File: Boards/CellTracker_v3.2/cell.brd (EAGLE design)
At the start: 41.9 x 41.9 mm, 24 parts, among them U2 LMR16020

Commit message: Changing antenna conf
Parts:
- moved U$8 2.17 mm to (40.3, 25.2), turned to 0 degrees
- moved U$7 1.80 mm to (28.7, 28.5)
- moved R2 0.57 mm to (20.7, 31.8)
- moved R6 0.57 mm to (20.7, 29.8)
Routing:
- net +3V3: track 61.2 -> 63.6 mm
- net N$1: track 5.25 -> 3.63 mm
- net N$4: track 3.62 -> 2.26 mm
- net N$3: track 3.29 -> 2.71 mm
- net RX3: track 13.5 -> 14.1 mm
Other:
- board size 41.9 x 41.9 mm -> 44.7 x 41.9 mm

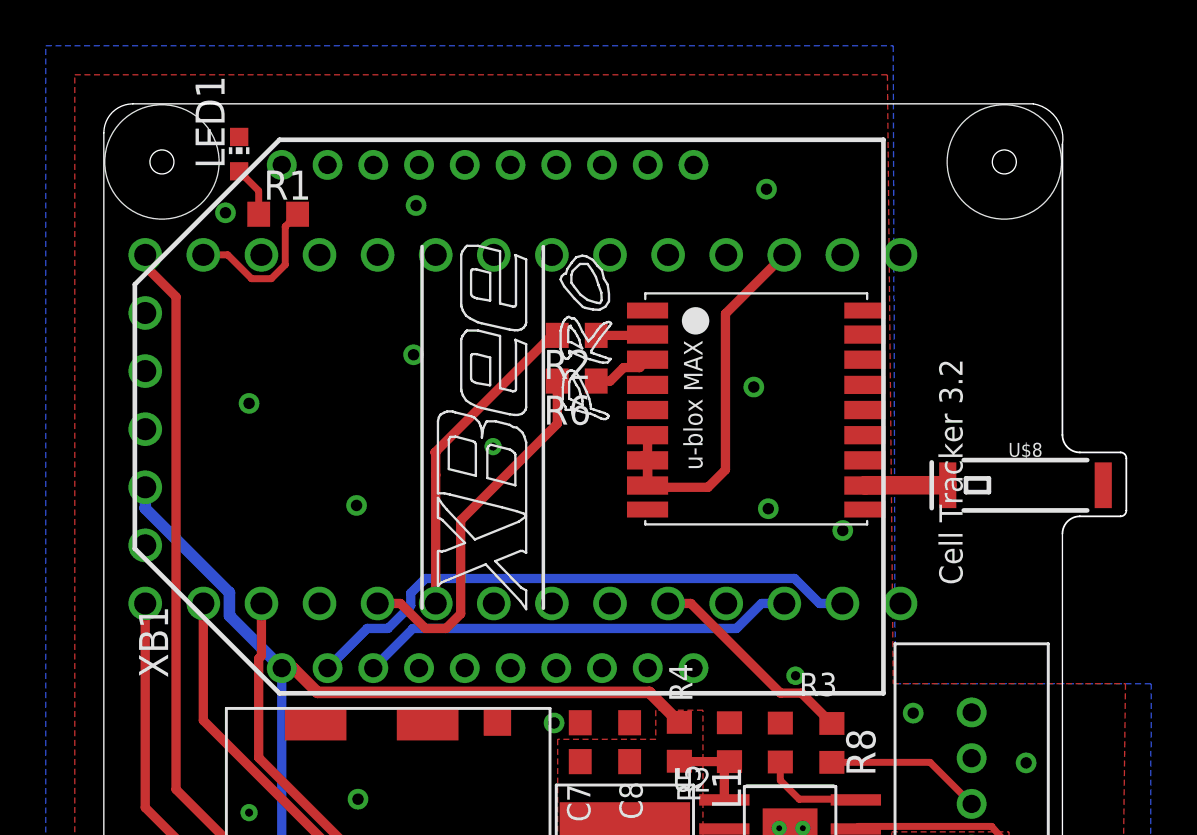
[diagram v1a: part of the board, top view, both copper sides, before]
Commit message: updating resistors for correct cutoff
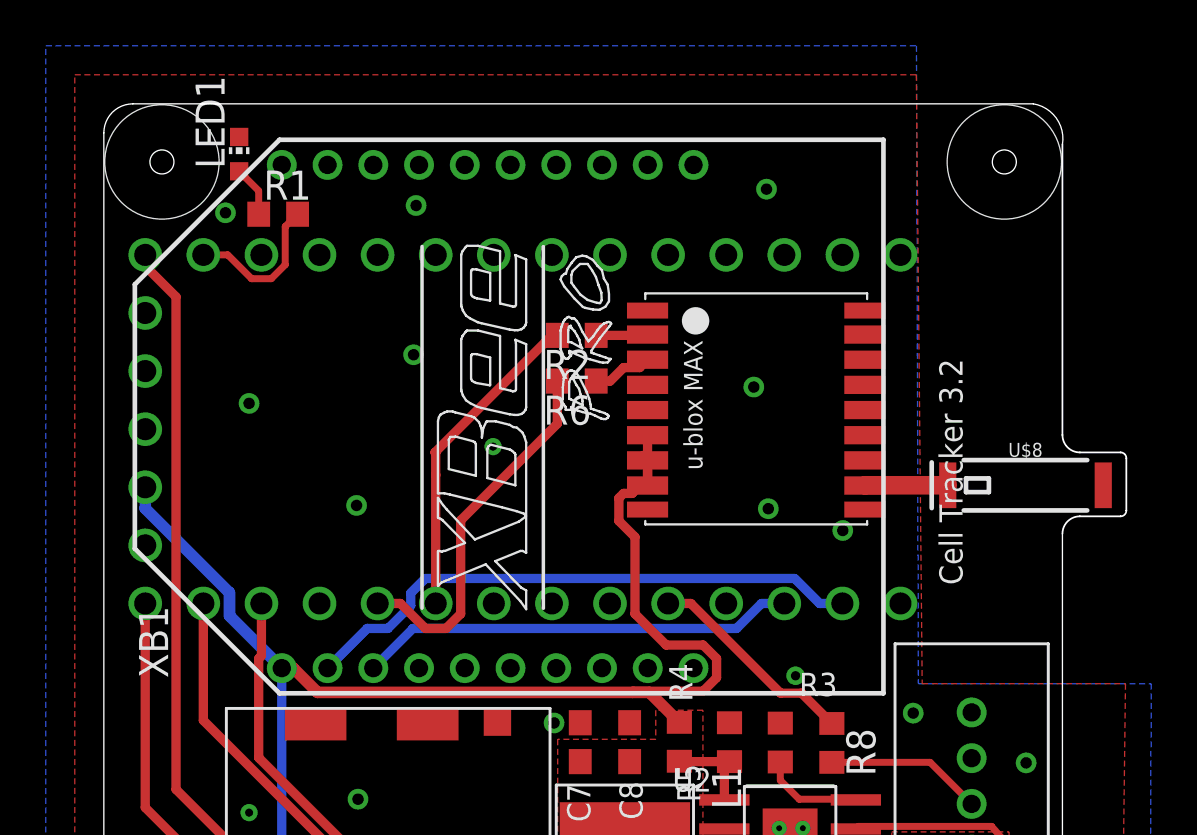
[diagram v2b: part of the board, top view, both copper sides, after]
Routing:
- net +3V3: track 63.6 -> 65.0 mm
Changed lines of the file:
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@@
 <polygon width="0.4064" layer="16" rank="6">
 <vertex x="-2.54" y="44.45"/>
-<vertex x="34.51225" y="44.45"/>
-<vertex x="34.597028125" y="16.557625"/>
+<vertex x="35.527478125" y="44.45"/>
+<vertex x="35.61225625" y="16.557625"/>
 <vertex x="45.792615625" y="16.557625"/>
 <vertex x="45.72" y="-2.54"/>
@@
 <polygon width="0.4064" layer="1" rank="6">
 <vertex x="-1.27" y="43.18"/>
-<vertex x="34.25825" y="43.18"/>
-<vertex x="34.513415625" y="16.557625"/>
+<vertex x="35.52338125" y="43.18"/>
+<vertex x="35.778546875" y="16.557625"/>
 <vertex x="44.66653125" y="16.557625"/>
 <vertex x="44.45" y="-1.27"/>
@@
 <contactref element="C7" pad="1"/>
 <contactref element="U$3" pad="VDD"/>
-<wire x1="23.77175" y1="26.32275" x2="23.77175" y2="25.146" width="0.4064" layer="1"/>
+<wire x1="23.77175" y1="25.146" x2="23.77175" y2="26.32275" width="0.4064" layer="1"/>
 <wire x1="23.77175" y1="26.32275" x2="23.77175" y2="27.42275" width="0.4064" layer="1"/>
 <wire x1="25.161875" y1="14.867625" x2="23.85065" y2="16.17885" width="0.508" layer="1"/>
 <wire x1="8.2803625" y1="17.23925" x2="7.78" y2="17.23925" width="0.508" layer="1"/>
-<wire x1="23.85065" y1="16.17885" x2="9.3407625" y2="16.17885" width="0.508" layer="1"/>
+<wire x1="23.85065" y1="16.17885" x2="23.114" y2="16.17885" width="0.508" layer="1"/>
+<wire x1="23.114" y1="16.17885" x2="9.3407625" y2="16.17885" width="0.508" layer="1"/>
 <wire x1="9.3407625" y1="16.17885" x2="8.2803625" y2="17.23925" width="0.508" layer="1"/>
 <wire x1="7.78" y1="17.23925" x2="7.78" y2="8.73" width="0.4064" layer="16"/>
@@
 <wire x1="5.492625" y1="19.526625" x2="5.492625" y2="20.5397" width="0.508" layer="16"/>
 <wire x1="5.492625" y1="20.5397" x2="1.809625" y2="24.2227" width="0.508" layer="16"/>
-<wire x1="29.749625" y1="35.30625" x2="27.178" y2="32.734625" width="0.4064" layer="1"/>
-<wire x1="27.178" y1="32.734625" x2="27.178" y2="25.908" width="0.4064" layer="1"/>
-<wire x1="27.178" y1="25.908" x2="26.416" y2="25.146" width="0.4064" layer="1"/>
-<wire x1="26.416" y1="25.146" x2="23.77175" y2="25.146" width="0.4064" layer="1"/>
-<wire x1="23.85065" y1="16.17885" x2="23.77175" y2="25.22275" width="0" layer="19" extent="1-1"/>
+<wire x1="26.19819375" y1="16.22965" x2="26.7896" y2="16.82105625" width="0.4064" layer="1"/>
+<wire x1="26.7896" y1="16.82105625" x2="26.7896" y2="17.65744375" width="0.4064" layer="1"/>
+<wire x1="26.7896" y1="17.65744375" x2="26.19819375" y2="18.24885" width="0.4064" layer="1"/>
+<wire x1="22.51615" y1="23.67545625" x2="22.51615" y2="24.67004375" width="0.4064" layer="1"/>
+<wire x1="22.51615" y1="24.67004375" x2="22.72445625" y2="24.87835" width="0.4064" layer="1"/>
+<wire x1="23.114" y1="16.17885" x2="23.1648" y2="16.22965" width="0.4064" layer="1"/>
+<wire x1="22.72445625" y1="24.87835" x2="23.10035" y2="24.87835" width="0.4064" layer="1"/>
+<wire x1="23.1648" y1="16.22965" x2="26.19819375" y2="16.22965" width="0.4064" layer="1"/>
+<wire x1="26.19819375" y1="18.24885" x2="24.58681875" y2="18.24885" width="0.4064" layer="1"/>
+<wire x1="24.58681875" y1="18.24885" x2="23.221825" y2="19.61384375" width="0.4064" layer="1"/>
+<wire x1="23.221825" y1="19.61384375" x2="23.221825" y2="22.96978125" width="0.4064" layer="1"/>
+<wire x1="23.221825" y1="22.96978125" x2="22.51615" y2="23.67545625" width="0.4064" layer="1"/>
+<wire x1="23.10035" y1="24.87835" x2="23.368" y2="25.146" width="0.4064" layer="1"/>
+<wire x1="23.77175" y1="27.42275" x2="29.749625" y2="35.30625" width="0" layer="19" extent="1-1"/>
+<wire x1="23.368" y1="25.146" x2="23.77175" y2="25.146" width="0" layer="19" extent="1-1"/>
+<wire x1="22.987" y1="13.15175" x2="25.161875" y2="14.867625" width="0" layer="19" extent="1-1"/>
+<wire x1="20.828" y1="13.15175" x2="22.987" y2="13.15175" width="0" layer="19" extent="1-1"/>
+<wire x1="22.780625" y1="10.528125" x2="22.987" y2="13.15175" width="0" layer="19" extent="1-1"/>
 </signal>
 <signal name="RX3">

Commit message: Code+nearly completed boards
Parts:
- added C1: (no value), jmolterLib:ELNASUPERCAP
- added D1: RB520S30T1G, diode:SOD523
- added R7: 22, resistor:R0603
- C6: value 47 uF -> 0.1 uF
- R10: value 195k -> 140k
- R4: value 45k -> 340k
- R5: value 13.3k -> 100k
- R9: value 45k -> 30.1k
- moved R6 0.08 mm to (20.7, 29.7)
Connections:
- new net N$11: D1.C, R7.2
- new net N$5: C1.3V3, R7.1, U$7.6_V_BCKP
- net +3V3: now also D1.A; no longer U$7.6_V_BCKP
- net GND: now also C1.GND
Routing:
- net +3V3: track 65.0 -> 79.8 mm
- net N$5: track 0.00 -> 14.4 mm, vias 0 -> 2
- net N$11: track 0.00 -> 1.98 mm
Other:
- outline, holes or cut-outs redrawn

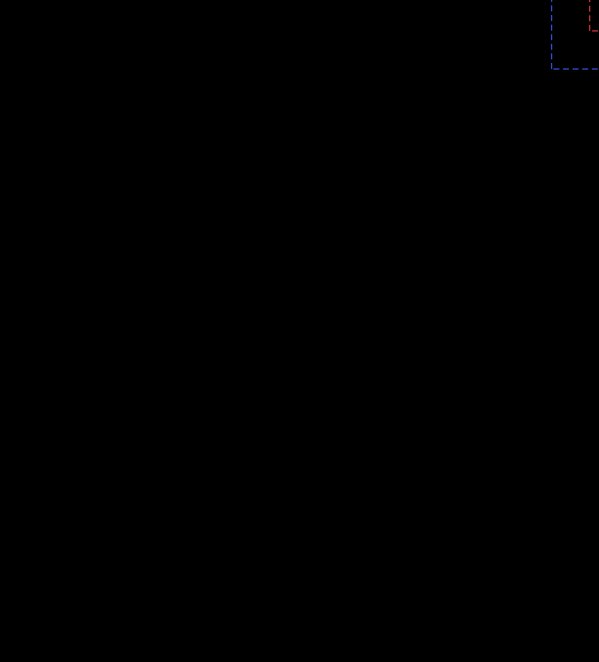
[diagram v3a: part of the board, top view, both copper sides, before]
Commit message: Moved libs, adding isolator
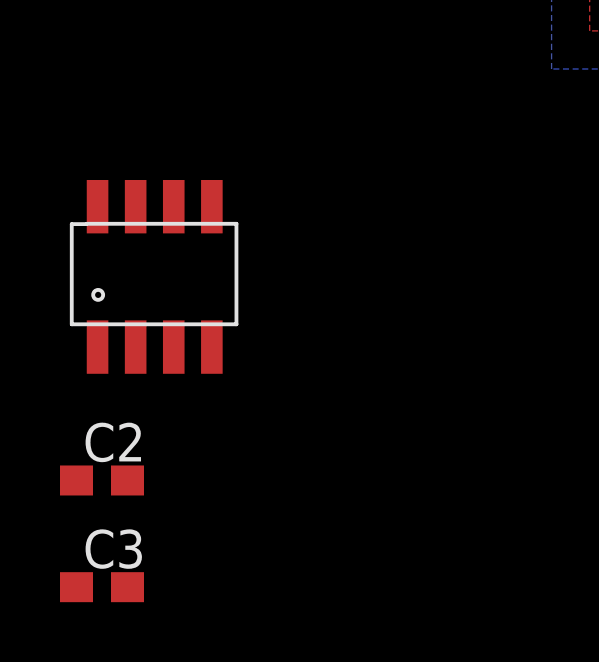
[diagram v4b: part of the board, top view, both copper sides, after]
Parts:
- added C2, C3: 0.1uF, rcl:C0603
- added ISO7021: ISO7021, jmolterLib:8-SOIC
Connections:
- removed net N$6: U$1.VIN
- new net GND_EX: C3.2, ISO7021.P$5
- new net IN_A: ISO7021.P$7
- new net IS_RX: ISO7021.P$2
- new net IS_TX: ISO7021.P$3
- new net OUT_B: ISO7021.P$6
- new net VCC_EX: C3.1, ISO7021.P$8
- net +3V3: now also C2.1, ISO7021.P$1
- net GND: now also C2.2, ISO7021.P$4
- net VIN: now also U$1.VIN
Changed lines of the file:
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@@
 <attribute name="VALUE" x="13.843" y="30.607" size="1.27" layer="27"/>
+</element>
+<element name="ISO7021" library="jmolterLib" package="8-SOIC" value="ISO7021" x="-18.034" y="-12.7" smashed="yes"/>
+<element name="C2" library="rcl" library_urn="urn:adsk.eagle:library:334" package="C0603" package3d_urn="urn:adsk.eagle:package:23616/2" value="0.1uF" x="-17.526" y="-16.256" smashed="yes">
+<attribute name="NAME" x="-18.161" y="-15.621" size="1.27" layer="25"/>
+<attribute name="SPICEPREFIX" value="C" x="-17.526" y="-16.256" size="1.778" layer="27" display="off"/>
+<attribute name="VALUE" x="-18.161" y="-18.161" size="1.27" layer="27"/>
+</element>
+<element name="C3" library="rcl" library_urn="urn:adsk.eagle:library:334" package="C0603" package3d_urn="urn:adsk.eagle:package:23616/2" value="0.1uF" x="-17.526" y="-19.812" smashed="yes">
+<attribute name="NAME" x="-18.161" y="-19.177" size="1.27" layer="25"/>
+<attribute name="SPICEPREFIX" value="C" x="-17.526" y="-19.812" size="1.778" layer="27" display="off"/>
+<attribute name="VALUE" x="-18.161" y="-21.717" size="1.27" layer="27"/>
 </element>
 </elements>
@@
 <via x="17.018" y="26.924" extent="1-16" drill="0.35"/>
 <contactref element="C1" pad="GND"/>
+<contactref element="ISO7021" pad="P$4"/>
+<contactref element="C2" pad="2"/>
+<wire x1="23.77175" y1="32.87275" x2="28.971875" y2="38.179375" width="0" layer="19" extent="1-1"/>
+<wire x1="28.41625" y1="29.5275" x2="23.77175" y2="32.87275" width="0" layer="19" extent="1-1"/>
+<wire x1="29.05125" y1="24.209375" x2="28.41625" y2="29.5275" width="0" layer="19" extent="1-1"/>
+<wire x1="32.305625" y1="23.256875" x2="29.05125" y2="24.209375" width="0" layer="19" extent="1-1"/>
+<wire x1="33.27175" y1="24.17275" x2="32.305625" y2="23.256875" width="0" layer="19" extent="1-1"/>
+<wire x1="33.27175" y1="26.32275" x2="33.27175" y2="24.17275" width="0" layer="19" extent="1-1"/>
+<wire x1="34.829625" y1="20.06625" x2="32.305625" y2="23.256875" width="0" layer="19" extent="1-1"/>
+<wire x1="35.385375" y1="15.27175" x2="34.829625" y2="20.06625" width="0" layer="19" extent="1-1"/>
+<wire x1="37.94125" y1="15.303125" x2="35.385375" y2="15.27175" width="0" layer="19" extent="1-1"/>
+<wire x1="37.94125" y1="13.303125" x2="37.94125" y2="15.303125" width="0" layer="19" extent="1-1"/>
+<wire x1="40.3225" y1="13.096875" x2="37.94125" y2="13.303125" width="0" layer="19" extent="1-1"/>
+<wire x1="29.575125" y1="14.835875" x2="35.385375" y2="15.27175" width="0" layer="19" extent="1-1"/>
+<wire x1="28.717875" y1="16.652875" x2="29.575125" y2="14.835875" width="0" layer="19" extent="1-1"/>
+<wire x1="27.352625" y1="14.85175" x2="29.575125" y2="14.835875" width="0" layer="19" extent="1-1"/>
+<wire x1="25.78" y1="17.23925" x2="27.352625" y2="14.85175" width="0" layer="19" extent="1-1"/>
+<wire x1="22.987" y1="14.85175" x2="25.78" y2="17.23925" width="0" layer="19" extent="1-1"/>
+<wire x1="20.828" y1="14.85175" x2="22.987" y2="14.85175" width="0" layer="19" extent="1-1"/>
+<wire x1="19.685" y1="14.843125" x2="20.828" y2="14.85175" width="0" layer="19" extent="1-1"/>
+<wire x1="17.2075" y1="14.878125" x2="19.685" y2="14.843125" width="0" layer="19" extent="1-1"/>
+<wire x1="14.1575" y1="14.778125" x2="17.2075" y2="14.878125" width="0" layer="19" extent="1-1"/>
+<wire x1="11.1125" y1="11.509375" x2="14.1575" y2="14.778125" width="0" layer="19" extent="1-1"/>
+<wire x1="9.2575" y1="14.778125" x2="11.1125" y2="11.509375" width="0" layer="19" extent="1-1"/>
+<wire x1="29.5275" y1="10.239375" x2="29.575125" y2="14.835875" width="0" layer="19" extent="1-1"/>
+<wire x1="29.5275" y1="9.445625" x2="29.5275" y2="10.239375" width="0" layer="19" extent="1-1"/>
+<wire x1="30.00375" y1="9.55675" x2="29.5275" y2="9.445625" width="0" layer="19" extent="1-1"/>
+<wire x1="30.559375" y1="9.445625" x2="30.00375" y2="9.55675" width="0" layer="19" extent="1-1"/>
+<wire x1="29.272625" y1="8.90675" x2="29.5275" y2="9.445625" width="0" layer="19" extent="1-1"/>
+<wire x1="30.559375" y1="10.239375" x2="30.559375" y2="9.445625" width="0" layer="19" extent="1-1"/>
+<wire x1="30.559375" y1="8.651875" x2="30.559375" y2="9.445625" width="0" layer="19" extent="1-1"/>
+<wire x1="6.35" y1="10.922" x2="11.1125" y2="11.509375" width="0" layer="19" extent="1-1"/>
+<wire x1="28.971875" y1="2.75925" x2="29.5275" y2="8.651875" width="0" layer="19" extent="1-1"/>
+<wire x1="32.131" y1="2.75925" x2="28.971875" y2="2.75925" width="0" layer="19" extent="1-1"/>
+<wire x1="34.471875" y1="2.778125" x2="32.131" y2="2.75925" width="0" layer="19" extent="1-1"/>
+<wire x1="6.111875" y1="4.7625" x2="6.35" y2="10.922" width="0" layer="19" extent="1-1"/>
+<wire x1="5.7575" y1="2.578125" x2="6.111875" y2="4.7625" width="0" layer="19" extent="1-1"/>
+<wire x1="10.16" y1="3.81" x2="6.111875" y2="4.7625" width="0" layer="19" extent="1-1"/>
+<wire x1="10.0575" y1="2.078125" x2="10.16" y2="3.81" width="0" layer="19" extent="1-1"/>
+<wire x1="20.9042" y1="4.524375" x2="27.12875" y2="8.90675" width="0" layer="19" extent="1-1"/>
+<wire x1="19.1075" y1="2.578125" x2="20.9042" y2="4.524375" width="0" layer="19" extent="1-1"/>
+<wire x1="17.018" y1="26.924" x2="23.77175" y2="32.87275" width="0" layer="19" extent="1-1"/>
+<wire x1="11.914" y1="27.748" x2="17.018" y2="26.924" width="0" layer="19" extent="1-1"/>
+<wire x1="11.049" y1="24.35225" x2="11.914" y2="27.748" width="0" layer="19" extent="1-1"/>
+<wire x1="13.541375" y1="30.940375" x2="11.914" y2="27.748" width="0" layer="19" extent="1-1"/>
+<wire x1="6.35" y1="28.813125" x2="11.914" y2="27.748" width="0" layer="19" extent="1-1"/>
+<wire x1="1.809625" y1="27.68625" x2="6.35" y2="28.813125" width="0" layer="19" extent="1-1"/>
+<wire x1="13.6525" y1="37.465" x2="13.541375" y2="30.940375" width="0" layer="19" extent="1-1"/>
+<wire x1="5.916125" y1="40.461125" x2="13.6525" y2="37.465" width="0" layer="19" extent="1-1"/>
+<wire x1="5.318125" y1="37.1475" x2="5.916125" y2="40.461125" width="0" layer="19" extent="1-1"/>
+<wire x1="-13.864" y1="-11.81" x2="5.7575" y2="2.578125" width="0" layer="19" extent="1-1"/>
+<wire x1="-16.676" y1="-16.256" x2="-13.864" y2="-11.81" width="0" layer="19" extent="1-1"/>
 </signal>
 <signal name="+3V3">
@@
 <wire x1="22.99210625" y1="25.146" x2="23.77175" y2="25.146" width="0.4064" layer="1"/>
 <wire x1="22.51615" y1="24.67004375" x2="22.99210625" y2="25.146" width="0.4064" layer="1"/>
+<contactref element="ISO7021" pad="P$1"/>
+<contactref element="C2" pad="1"/>
 <wire x1="23.77175" y1="26.32275" x2="17.50203125" y2="34.21405" width="0" layer="19" extent="1-1"/>
+<wire x1="22.987" y1="13.15175" x2="25.161875" y2="14.867625" width="0" layer="19" extent="1-1"/>
+<wire x1="20.828" y1="13.15175" x2="22.987" y2="13.15175" width="0" layer="19" extent="1-1"/>
+<wire x1="22.780625" y1="10.528125" x2="22.987" y2="13.15175" width="0" layer="19" extent="1-1"/>
+<wire x1="-17.674" y1="-11.81" x2="7.78" y2="8.73" width="0" layer="19" extent="1-16"/>
+<wire x1="-18.376" y1="-16.256" x2="-17.674" y2="-11.81" width="0" layer="19" extent="1-1"/>
 </signal>
 <signal name="RX3">
@@
 <contactref element="C10" pad="1"/>
 <contactref element="C9" pad="1"/>
+<contactref element="U$1" pad="VIN"/>
+<wire x1="37.94125" y1="9.303125" x2="34.829625" y2="35.30625" width="0" layer="19" extent="1-1"/>
+<wire x1="32.87875" y1="8.90675" x2="37.94125" y2="9.303125" width="0" layer="19" extent="1-1"/>
+<wire x1="32.131" y1="5.55925" x2="32.87875" y2="8.90675" width="0" layer="19" extent="1-1"/>
+<wire x1="34.471875" y1="5.000625" x2="32.131" y2="5.55925" width="0" layer="19" extent="1-1"/>
+<wire x1="28.971875" y1="5.55925" x2="32.131" y2="5.55925" width="0" layer="19" extent="1-1"/>
 </signal>
 <signal name="N$17">
@@
 </signal>
 <signal name="N$54">
-</signal>
-<signal name="N$6">
-<contactref element="U$1" pad="VIN"/>
 </signal>
 <signal name="SWITCH_LED">
@@
 <wire x1="12.026" y1="32.512" x2="13.878" y2="32.512" width="0.4064" layer="1"/>
 </signal>
+<signal name="IS_RX">
+<contactref element="ISO7021" pad="P$2"/>
+</signal>
+<signal name="IS_TX">
+<contactref element="ISO7021" pad="P$3"/>
+</signal>
+<signal name="IN_A">
+<contactref element="ISO7021" pad="P$7"/>
+</signal>
+<signal name="OUT_B">
+<contactref element="ISO7021" pad="P$6"/>
+</signal>
+<signal name="GND_EX">
+<contactref element="C3" pad="2"/>
+<contactref element="ISO7021" pad="P$5"/>
+<wire x1="-13.864" y1="-7.13" x2="-16.676" y2="-19.812" width="0" layer="19" extent="1-1"/>
+</signal>
+<signal name="VCC_EX">
+<contactref element="C3" pad="1"/>
+<contactref element="ISO7021" pad="P$8"/>
+<wire x1="-17.674" y1="-7.13" x2="-18.376" y2="-19.812" width="0" layer="19" extent="1-1"/>
+</signal>
 </signals>
